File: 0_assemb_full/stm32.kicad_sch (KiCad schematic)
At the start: 28 parts, among them J10 SPIConn_01x03, J9 Conn_02x05_Odd_Even, SW1 SW_Push, U5 STM32F091RCTx, U7 MAX7375AXR805

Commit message: Additional changes
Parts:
- C13, C17, C19: footprint Capacitor_THT:CP_Radial_D5.0mm_P2.50mm -> Capacitor_SMD:C_0805_2012Metric_Pad1.18x1.45mm_HandSolder
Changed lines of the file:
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@@
       (effects (font (size 1.27 1.27)) (justify left))
     )
-    (property "Footprint" "Capacitor_THT:CP_Radial_D5.0mm_P2.50mm" (id 2) (at 32.7152 29.21 0)
+    (property "Footprint" "Capacitor_SMD:C_0805_2012Metric_Pad1.18x1.45mm_HandSolder" (id 2) (at 32.7152 29.21 0)
       (effects (font (size 1.27 1.27)) hide)
     )
@@
       (effects (font (size 1.27 1.27)) (justify left))
     )
-    (property "Footprint" "Capacitor_THT:CP_Radial_D5.0mm_P2.50mm" (id 2) (at 46.6852 73.66 0)
+    (property "Footprint" "Capacitor_SMD:C_0805_2012Metric_Pad1.18x1.45mm_HandSolder" (id 2) (at 46.6852 73.66 0)
       (effects (font (size 1.27 1.27)) hide)
     )
@@
       (effects (font (size 1.27 1.27)) (justify left))
     )
-    (property "Footprint" "Capacitor_THT:CP_Radial_D5.0mm_P2.50mm" (id 2) (at 32.7152 49.53 0)
-      (effects (font (size 1.27 1.27)) hide)
-    )
+    (property "Footprint" "Capacitor_SMD:C_0805_2012Metric_Pad1.18x1.45mm_HandSolder" (id 2) (at 32.7152 49.53 0)
+      (effects (font (size 1.27 1.27)) hide)
+    )

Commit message: Some filter adjustments
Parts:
- J9: value Conn_02x05_Odd_Even -> ProgHeader
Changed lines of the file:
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@@
     (in_bom yes) (on_board yes)
     (property "Reference" "J9" (id 0) (at 50.8 111.9886 0))
-    (property "Value" "Conn_02x05_Odd_Even" (id 1) (at 50.8 114.3 0))
+    (property "Value" "ProgHeader" (id 1) (at 50.8 114.3 0))
     (property "Footprint" "Connector_PinHeader_2.54mm:PinHeader_2x02_P2.54mm_Vertical" (id 2) (at 49.53 118.11 0)
       (effects (font (size 1.27 1.27)) hide)

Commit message: Active Filters layout added
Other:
- title: (none) -> STM32 Interfacing
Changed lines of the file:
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@@
 (kicad_sch (version 20211123) (generator eeschema)
   (paper "A4")
+  (title_block
+    (title "STM32 Interfacing")
+  )
   (junction (at 38.1 50.8) (diameter 0) (color 0 0 0 0)
   )

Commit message: Final adjustments
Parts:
- added J13: RPiConn_01x03, Connector_PinSocket_2.54mm:PinSocket_1x03_P2.54mm_Vertical, symbol Connector_Generic:Conn_01x03
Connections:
- net GPIO1: now reaches U5.59 (PB7)
- net GPIO1: now also J13.1 (Pin_1)
- net GPIO2: now reaches U5.61 (PB8)
- net GPIO2: now also J13.2 (Pin_2)
- net GPIO3: now reaches U5.62 (PB9)
- net GPIO3: now also J13.3 (Pin_3)
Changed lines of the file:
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@@
+    (stroke (width 0) (type default) (color 0 0 0 0))
+  )
+  (wire (pts (xy 152.4 116.84) (xy 166.37 116.84))
     (stroke (width 0) (type default) (color 0 0 0 0))
   )
@@
     (stroke (width 0) (type default) (color 0 0 0 0))
   )
+  (wire (pts (xy 189.23 119.38) (xy 195.58 119.38))
+    (stroke (width 0) (type default) (color 0 0 0 0))
+  )
   (wire (pts (xy 25.4 20.32) (xy 31.75 20.32))
     (stroke (width 0) (type default) (color 0 0 0 0))
@@
     (stroke (width 0) (type default) (color 0 0 0 0))
   )
+  (wire (pts (xy 152.4 119.38) (xy 166.37 119.38))
+    (stroke (width 0) (type default) (color 0 0 0 0))
+  )
   (wire (pts (xy 152.4 78.74) (xy 162.56 78.74))
     (stroke (width 0) (type default) (color 0 0 0 0))
@@
     (stroke (width 0) (type default) (color 0 0 0 0))
   )
+  (wire (pts (xy 152.4 114.3) (xy 166.37 114.3))
+    (stroke (width 0) (type default) (color 0 0 0 0))
+  )
   (wire (pts (xy 185.42 129.54) (xy 195.58 129.54))
     (stroke (width 0) (type default) (color 0 0 0 0))
@@
     (stroke (width 0) (type default) (color 0 0 0 0))
   )
+  (wire (pts (xy 189.23 114.3) (xy 195.58 114.3))
+    (stroke (width 0) (type default) (color 0 0 0 0))
+  )
   (wire (pts (xy 185.42 132.08) (xy 195.58 132.08))
     (stroke (width 0) (type default) (color 0 0 0 0))
@@
   )
   (wire (pts (xy 113.03 53.34) (xy 119.38 53.34))
+    (stroke (width 0) (type default) (color 0 0 0 0))
+  )
+  (wire (pts (xy 189.23 116.84) (xy 195.58 116.84))
     (stroke (width 0) (type default) (color 0 0 0 0))
   )
@@
     (effects (font (size 1.27 1.27)) (justify left bottom))
   )
+  (label "GPIO3" (at 189.23 119.38 0)
+    (effects (font (size 1.27 1.27)) (justify left bottom))
+  )
   (label "SPI_MOSI" (at 166.37 134.62 180)
     (effects (font (size 1.27 1.27)) (justify right bottom))
@@
     (effects (font (size 1.27 1.27)) (justify right bottom))
   )
+  (label "GPIO2" (at 166.37 116.84 180)
+    (effects (font (size 1.27 1.27)) (justify right bottom))
+  )
+  (label "GPIO3" (at 166.37 119.38 180)
+    (effects (font (size 1.27 1.27)) (justify right bottom))
+  )
   (label "NRST" (at 113.03 53.34 0)
     (effects (font (size 1.27 1.27)) (justify left bottom))
@@
     (effects (font (size 1.27 1.27)) (justify right bottom))
   )
+  (label "GPIO1" (at 189.23 114.3 0)
+    (effects (font (size 1.27 1.27)) (justify left bottom))
+  )
   (label "EClock" (at 107.95 81.28 0)
     (effects (font (size 1.27 1.27)) (justify left bottom))
@@
     (effects (font (size 1.27 1.27)) (justify left bottom))
   )
+  (label "GPIO2" (at 189.23 116.84 0)
+    (effects (font (size 1.27 1.27)) (justify left bottom))
+  )
   (label "SPI_NSS" (at 166.37 127 180)
     (effects (font (size 1.27 1.27)) (justify right bottom))
@@
   )
   (label "VDDA" (at 64.77 64.77 180)
+    (effects (font (size 1.27 1.27)) (justify right bottom))
+  )
+  (label "GPIO1" (at 166.37 114.3 180)
     (effects (font (size 1.27 1.27)) (justify right bottom))
   )
@@
     (pin "1")
   )
+  (symbol (lib_id "Connector_Generic:Conn_01x03") (at 200.66 116.84 0) (unit 1)
+    (in_bom yes) (on_board yes) (fields_autoplaced)
+    (property "Reference" "J13" (id 0) (at 203.2 115.5699 0)
+      (effects (font (size 1.27 1.27)) (justify left))
+    )
+    (property "Value" "RPiConn_01x03" (id 1) (at 203.2 118.1099 0)
+      (effects (font (size 1.27 1.27)) (justify left))
+    )
+    (property "Footprint" "Connector_PinSocket_2.54mm:PinSocket_1x03_P2.54mm_Vertical" (id 2) (at 200.66 116.84 0)
+      (effects (font (size 1.27 1.27)) hide)
+    )
+    (property "Datasheet" "~" (id 3) (at 200.66 116.84 0)
+      (effects (font (size 1.27 1.27)) hide)
+    )
+    (pin "1")
+    (pin "2")
+    (pin "3")
+  )
   (symbol (lib_id "Device:C") (at 59.69 25.4 0) (unit 1)

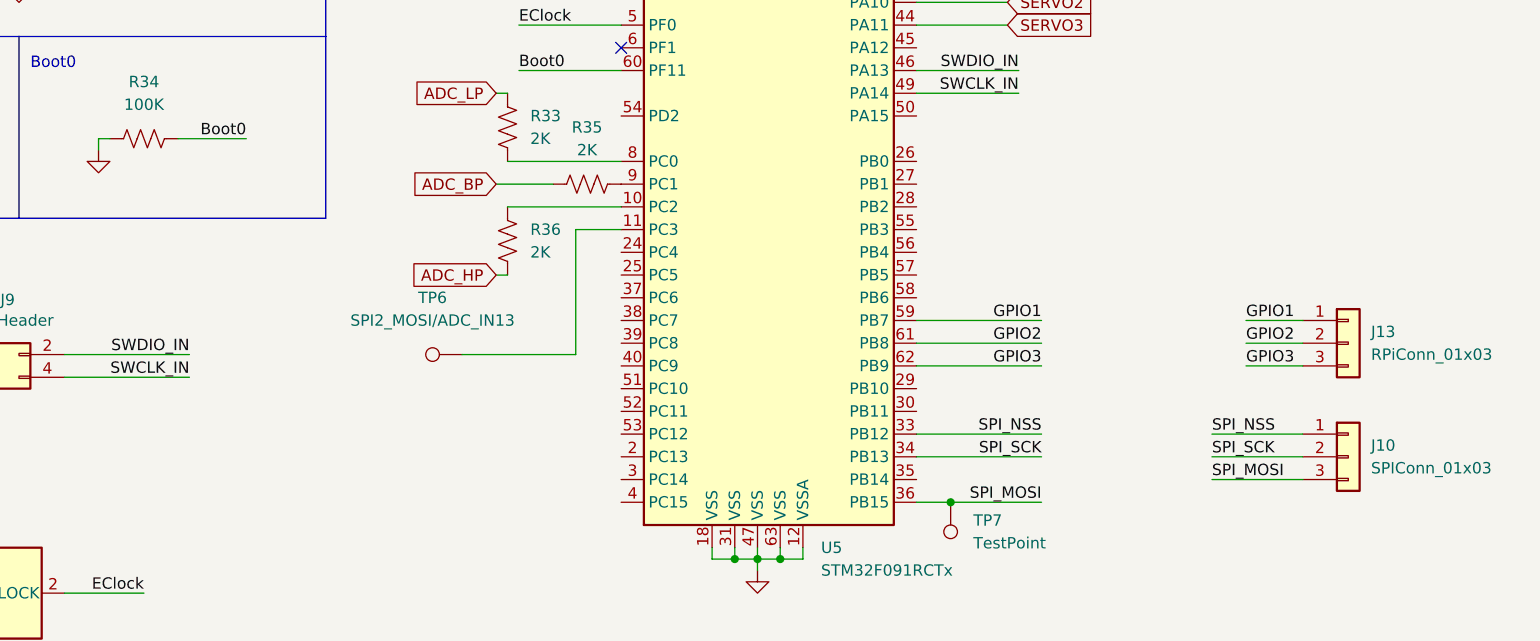
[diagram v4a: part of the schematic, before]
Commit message: Final adjustments (mostly silkscreen) pre-presentation
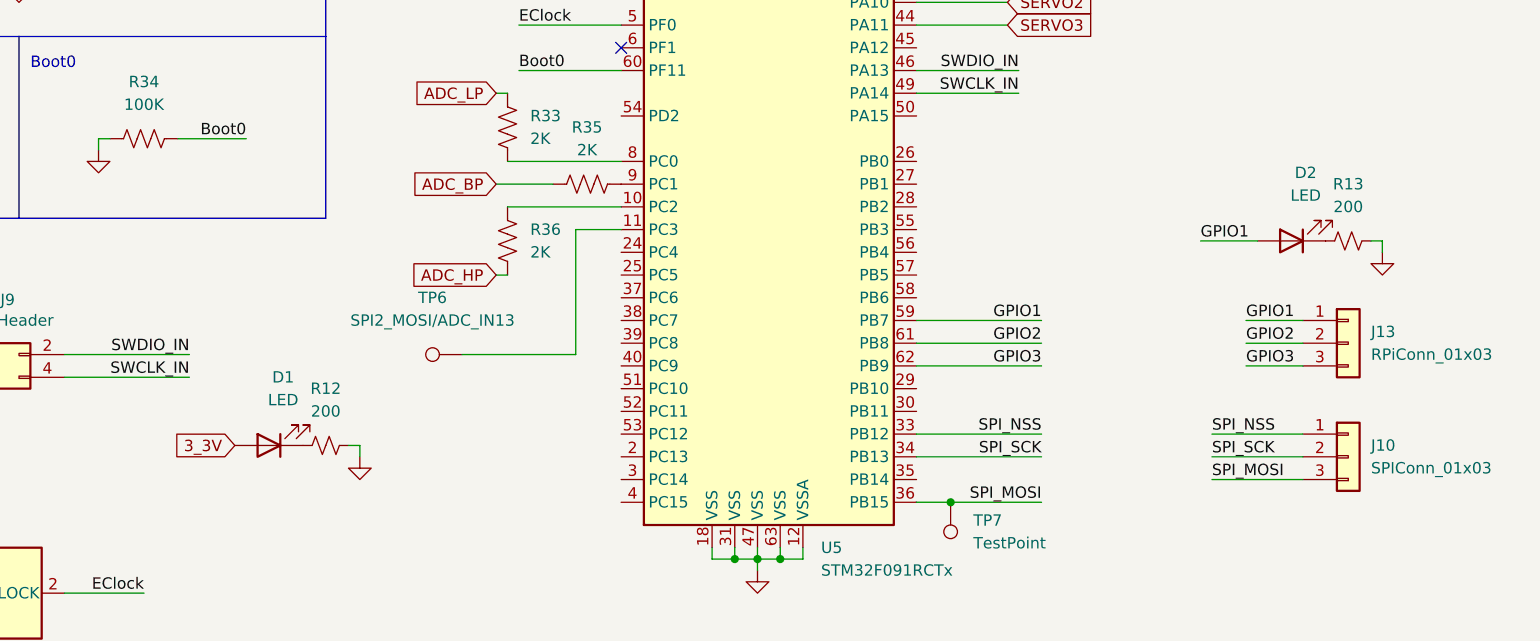
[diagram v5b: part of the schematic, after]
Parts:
- added D1, D2: LED, LED_SMD:LED_0805_2012Metric_Pad1.15x1.40mm_HandSolder, symbol Device:LED
- added R12, R13: 200, Resistor_SMD:R_0805_2012Metric_Pad1.20x1.40mm_HandSolder, symbol Device:R_Small_US
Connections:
- net 3_3V: now also D1.2 (A)
- net GND: now also R12.2, R13.2
- net GPIO1: now also D2.2 (A)
- new net: D2.1 (K), R13.1
- new net: D1.1 (K), R12.1
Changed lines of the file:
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@@
+    (stroke (width 0) (type default) (color 0 0 0 0))
+  )
+  (wire (pts (xy 90.17 129.54) (xy 90.17 128.27))
     (stroke (width 0) (type default) (color 0 0 0 0))
   )
@@
     (stroke (width 0) (type default) (color 0 0 0 0))
   )
+  (wire (pts (xy 184.15 105.41) (xy 190.5 105.41))
+    (stroke (width 0) (type default) (color 0 0 0 0))
+  )
   (polyline (pts (xy 86.36 102.87) (xy 86.36 82.55))
     (stroke (width 0) (type default) (color 0 0 0 0))
@@
     (stroke (width 0) (type default) (color 0 0 0 0))
   )
+  (wire (pts (xy 204.47 105.41) (xy 203.2 105.41))
+    (stroke (width 0) (type default) (color 0 0 0 0))
+  )
   (wire (pts (xy 38.1 50.8) (xy 45.72 50.8))
     (stroke (width 0) (type default) (color 0 0 0 0))
@@
     (stroke (width 0) (type default) (color 0 0 0 0))
   )
+  (wire (pts (xy 90.17 128.27) (xy 88.9 128.27))
+    (stroke (width 0) (type default) (color 0 0 0 0))
+  )
   (wire (pts (xy 31.75 30.48) (xy 45.72 30.48))
     (stroke (width 0) (type default) (color 0 0 0 0))
@@
   )
   (wire (pts (xy 129.54 46.99) (xy 128.27 46.99))
+    (stroke (width 0) (type default) (color 0 0 0 0))
+  )
+  (wire (pts (xy 204.47 106.68) (xy 204.47 105.41))
     (stroke (width 0) (type default) (color 0 0 0 0))
   )
@@
   (label "VDD_In" (at 80.01 20.32 180)
     (effects (font (size 1.27 1.27)) (justify right bottom))
+  )
+  (label "GPIO1" (at 184.15 105.41 0)
+    (effects (font (size 1.27 1.27)) (justify left bottom))
   )
   (label "VDDA" (at 64.77 64.77 180)
@@
     )
   )
+  (global_label "3_3V" (shape input) (at 76.2 128.27 180) (fields_autoplaced)
+    (effects (font (size 1.27 1.27)) (justify right))
+    (property "Intersheet References" "${INTERSHEET_REFS}" (id 0) (at 69.3117 128.3494 0)
+      (effects (font (size 1.27 1.27)) (justify right) hide)
+    )
+  )
   (global_label "3_3V" (shape input) (at 25.4 20.32 180) (fields_autoplaced)
     (effects (font (size 1.27 1.27)) (justify right))
@@
     (pin "1")
   )
+  (symbol (lib_id "power:GND") (at 90.17 129.54 0) (unit 1)
+    (in_bom yes) (on_board yes)
+    (property "Reference" "#PWR014" (id 0) (at 90.17 135.89 0)
+      (effects (font (size 1.27 1.27)) hide)
+    )
+    (property "Value" "GND" (id 1) (at 90.297 133.9342 0)
+      (effects (font (size 1.27 1.27)) hide)
+    )
+    (property "Footprint" "" (id 2) (at 90.17 129.54 0)
+      (effects (font (size 1.27 1.27)) hide)
+    )
+    (property "Datasheet" "" (id 3) (at 90.17 129.54 0)
+      (effects (font (size 1.27 1.27)) hide)
+    )
+    (pin "1")
+  )
+  (symbol (lib_id "Device:R_Small_US") (at 200.66 105.41 90) (unit 1)
+    (in_bom yes) (on_board yes) (fields_autoplaced)
+    (property "Reference" "R13" (id 0) (at 200.66 99.06 90))
+    (property "Value" "200" (id 1) (at 200.66 101.6 90))
+    (property "Footprint" "Resistor_SMD:R_0805_2012Metric_Pad1.20x1.40mm_HandSolder" (id 2) (at 200.66 105.41 0)
+      (effects (font (size 1.27 1.27)) hide)
+    )
+    (property "Datasheet" "~" (id 3) (at 200.66 105.41 0)
+      (effects (font (size 1.27 1.27)) hide)
+    )
+    (pin "1")
+    (pin "2")
+  )
   (symbol (lib_id "Connector_Generic:Conn_01x03") (at 200.66 116.84 0) (unit 1)
     (in_bom yes) (on_board yes) (fields_autoplaced)
@@
     (pin "3")
   )
+  (symbol (lib_id "Device:R_Small_US") (at 86.36 128.27 90) (unit 1)
+    (in_bom yes) (on_board yes) (fields_autoplaced)
+    (property "Reference" "R12" (id 0) (at 86.36 121.92 90))
+    (property "Value" "200" (id 1) (at 86.36 124.46 90))
+    (property "Footprint" "Resistor_SMD:R_0805_2012Metric_Pad1.20x1.40mm_HandSolder" (id 2) (at 86.36 128.27 0)
+      (effects (font (size 1.27 1.27)) hide)
+    )
+    (property "Datasheet" "~" (id 3) (at 86.36 128.27 0)
+      (effects (font (size 1.27 1.27)) hide)
+    )
+    (pin "1")
+    (pin "2")
+  )
   (symbol (lib_id "Device:C") (at 59.69 25.4 0) (unit 1)
     (in_bom yes) (on_board yes) (fields_autoplaced)
@@
     )
     (pin "1")
+  )
+  (symbol (lib_id "Device:LED") (at 80.01 128.27 180) (unit 1)
+    (in_bom yes) (on_board yes) (fields_autoplaced)
+    (property "Reference" "D1" (id 0) (at 81.5975 120.65 0))
+    (property "Value" "LED" (id 1) (at 81.5975 123.19 0))
+    (property "Footprint" "LED_SMD:LED_0805_2012Metric_Pad1.15x1.40mm_HandSolder" (id 2) (at 80.01 128.27 0)
+      (effects (font (size 1.27 1.27)) hide)
+    )
+    (property "Datasheet" "~" (id 3) (at 80.01 128.27 0)
+      (effects (font (size 1.27 1.27)) hide)
+    )
+    (pin "1")
+    (pin "2")
   )
   (symbol (lib_id "power:GND") (at 43.18 96.52 0) (unit 1)
@@
     (pin "1")
   )
+  (symbol (lib_id "Device:LED") (at 194.31 105.41 180) (unit 1)
+    (in_bom yes) (on_board yes) (fields_autoplaced)
+    (property "Reference" "D2" (id 0) (at 195.8975 97.79 0))
+    (property "Value" "LED" (id 1) (at 195.8975 100.33 0))
+    (property "Footprint" "LED_SMD:LED_0805_2012Metric_Pad1.15x1.40mm_HandSolder" (id 2) (at 194.31 105.41 0)
+      (effects (font (size 1.27 1.27)) hide)
+    )
+    (property "Datasheet" "~" (id 3) (at 194.31 105.41 0)
+      (effects (font (size 1.27 1.27)) hide)
+    )
+    (pin "1")
+    (pin "2")
+  )
   (symbol (lib_id "Device:R_US") (at 115.57 99.06 90) (unit 1)
     (in_bom yes) (on_board yes) (fields_autoplaced)
@@
     (pin "2")
   )
+  (symbol (lib_id "power:GND") (at 204.47 106.68 0) (unit 1)
+    (in_bom yes) (on_board yes)
+    (property "Reference" "#PWR049" (id 0) (at 204.47 113.03 0)
+      (effects (font (size 1.27 1.27)) hide)
+    )
+    (property "Value" "GND" (id 1) (at 204.597 111.0742 0)
+      (effects (font (size 1.27 1.27)) hide)
+    )
+    (property "Footprint" "" (id 2) (at 204.47 106.68 0)
+      (effects (font (size 1.27 1.27)) hide)
+    )
+    (property "Datasheet" "" (id 3) (at 204.47 106.68 0)
+      (effects (font (size 1.27 1.27)) hide)
+    )
+    (pin "1")
+  )
   (symbol (lib_id "power:GND") (at 134.62 142.24 0) (unit 1)

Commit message: Made adjustments according to presentation feedback. Almost ready for teaching team to look over.
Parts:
- removed J13: RPiConn_01x03, Connector_PinSocket_2.54mm:PinSocket_1x03_P2.54mm_Vertical, symbol Connector_Generic:Conn_01x03
- added TP12: GPIO1, TestPoint:TestPoint_THTPad_2.0x2.0mm_Drill1.0mm, symbol Connector:TestPoint
- added TP13: GPIO4, TestPoint:TestPoint_THTPad_2.0x2.0mm_Drill1.0mm, symbol Connector:TestPoint
- added TP14: GPIO2, TestPoint:TestPoint_THTPad_2.0x2.0mm_Drill1.0mm, symbol Connector:TestPoint
- added TP15: GPIO5, TestPoint:TestPoint_THTPad_2.0x2.0mm_Drill1.0mm, symbol Connector:TestPoint
- added TP16: GPIO3, TestPoint:TestPoint_THTPad_2.0x2.0mm_Drill1.0mm, symbol Connector:TestPoint
- added TP17: GPIO6, TestPoint:TestPoint_THTPad_2.0x2.0mm_Drill1.0mm, symbol Connector:TestPoint
- TP7: value TestPoint -> MOSI; footprint TestPoint:TestPoint_THTPad_1.5x1.5mm_Drill0.7mm -> TestPoint:TestPoint_THTPad_2.0x2.0mm_Drill1.0mm
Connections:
- net GPIO1: now also U5.56 (PB4), TP12.1; no longer U5.59 (PB7)
- net GPIO2: now also U5.57 (PB5), TP14.1; no longer U5.61 (PB8)
- net GPIO3: now also U5.58 (PB6), TP16.1; no longer U5.62 (PB9)
- new net GPIO4: TP13.1, U5.59 (PB7)
- new net GPIO5: TP15.1, U5.61 (PB8)
- new net GPIO6: TP17.1, U5.62 (PB9)
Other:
- moved on the sheet: J10

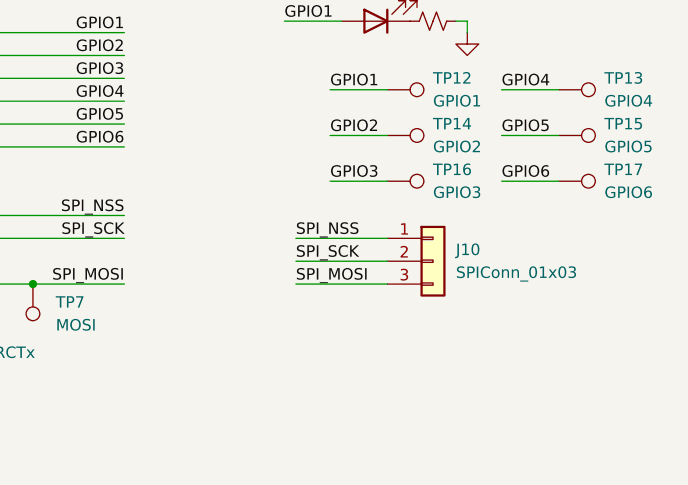
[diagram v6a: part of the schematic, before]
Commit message: Fixed LED Board and added GND to SPI on Main Board
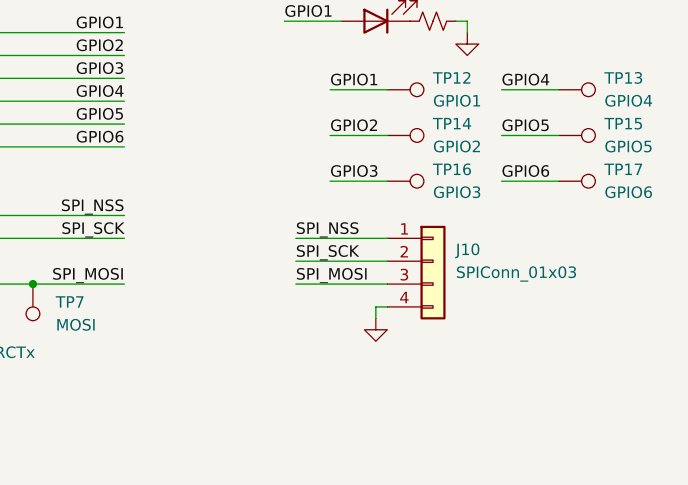
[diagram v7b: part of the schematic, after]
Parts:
- J10: footprint Connector_PinSocket_2.54mm:PinSocket_1x03_P2.54mm_Vertical -> Connector_PinHeader_2.54mm:PinHeader_1x04_P2.54mm_Vertical; symbol Connector_Generic:Conn_01x03 -> Connector_Generic:Conn_01x04
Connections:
- net GND: now also J10.4 (Pin_4)
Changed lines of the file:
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@@
+    (stroke (width 0) (type default) (color 0 0 0 0))
+  )
+  (wire (pts (xy 194.31 138.43) (xy 194.31 137.16))
     (stroke (width 0) (type default) (color 0 0 0 0))
   )
@@
   )
   (polyline (pts (xy 52.07 82.55) (xy 52.07 102.87))
+    (stroke (width 0) (type default) (color 0 0 0 0))
+  )
+  (wire (pts (xy 194.31 137.16) (xy 195.58 137.16))
     (stroke (width 0) (type default) (color 0 0 0 0))
   )
@@
     (pin "1")
   )
-  (symbol (lib_id "Connector_Generic:Conn_01x03") (at 200.66 132.08 0) (unit 1)
+  (symbol (lib_id "Connector_Generic:Conn_01x04") (at 200.66 132.08 0) (unit 1)
     (in_bom yes) (on_board yes) (fields_autoplaced)
     (property "Reference" "J10" (id 0) (at 203.2 130.8099 0)
@@
       (effects (font (size 1.27 1.27)) (justify left))
     )
-    (property "Footprint" "Connector_PinSocket_2.54mm:PinSocket_1x03_P2.54mm_Vertical" (id 2) (at 200.66 132.08 0)
+    (property "Footprint" "Connector_PinHeader_2.54mm:PinHeader_1x04_P2.54mm_Vertical" (id 2) (at 200.66 132.08 0)
       (effects (font (size 1.27 1.27)) hide)
     )
@@
     (pin "2")
     (pin "3")
+    (pin "4")
   )
   (symbol (lib_id "Device:C") (at 31.75 25.4 0) (unit 1)
@@
     (pin "2")
   )
+  (symbol (lib_id "power:GND") (at 194.31 138.43 0) (unit 1)
+    (in_bom yes) (on_board yes)
+    (property "Reference" "#PWR0103" (id 0) (at 194.31 144.78 0)
+      (effects (font (size 1.27 1.27)) hide)
+    )
+    (property "Value" "GND" (id 1) (at 194.437 142.8242 0)
+      (effects (font (size 1.27 1.27)) hide)
+    )
+    (property "Footprint" "" (id 2) (at 194.31 138.43 0)
+      (effects (font (size 1.27 1.27)) hide)
+    )
+    (property "Datasheet" "" (id 3) (at 194.31 138.43 0)
+      (effects (font (size 1.27 1.27)) hide)
+    )
+    (pin "1")
+  )
   (symbol (lib_id "Device:FerriteBead") (at 31.75 64.77 90) (unit 1)
